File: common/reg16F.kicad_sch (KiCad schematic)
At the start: 8 parts, among them U10 SN74AHCT16374DGGR, U11 74AHC1G08

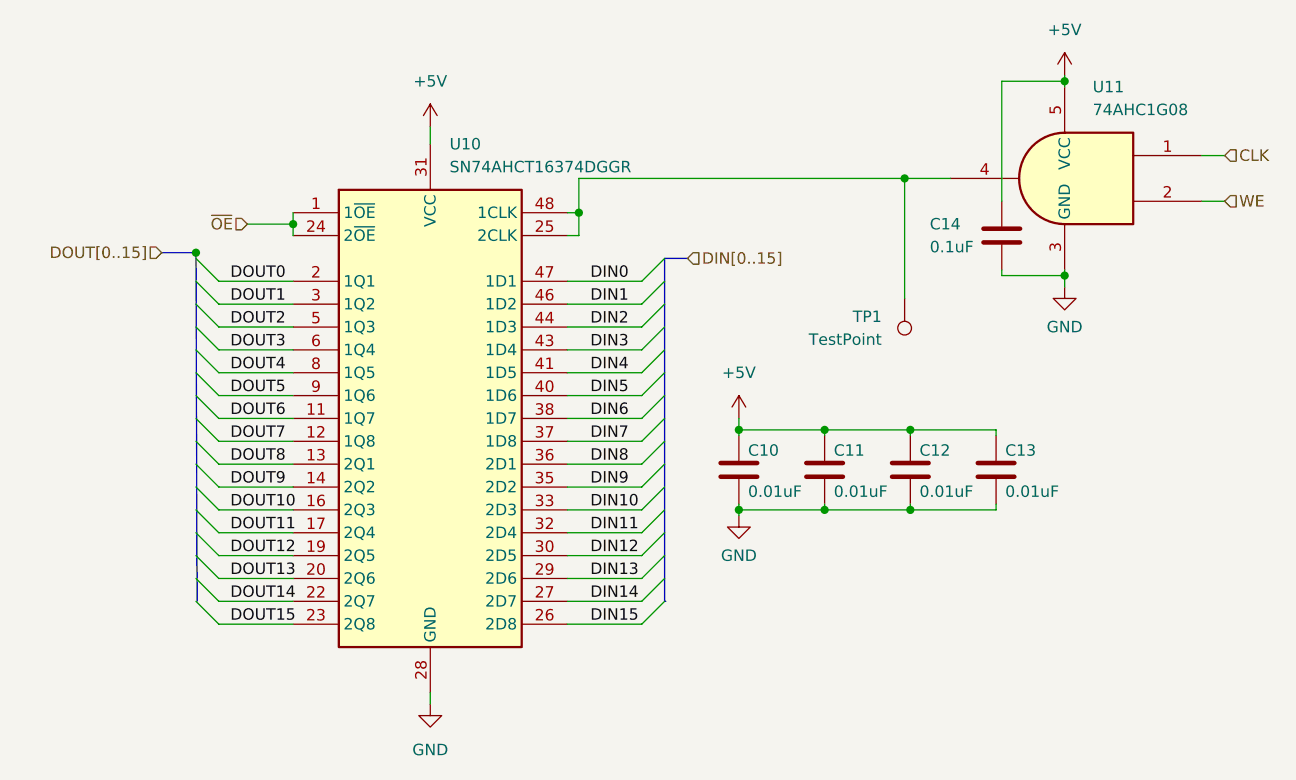
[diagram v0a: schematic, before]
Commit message: Cleanup, added photos and README overhaul
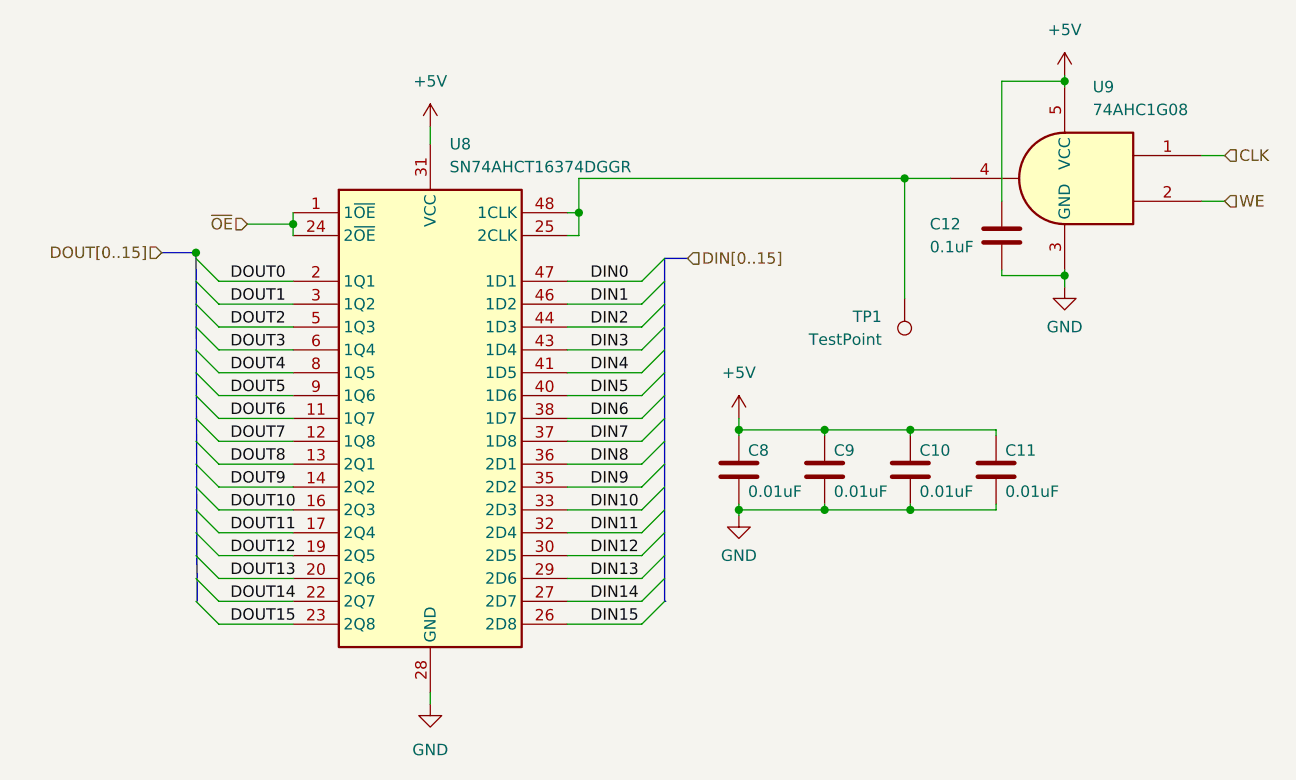
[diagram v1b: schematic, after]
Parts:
- renumbered C12 to C10, C13 to C11, C14 to C12, C10 to C8, C11 to C9, U10 to U8, U11 to U9
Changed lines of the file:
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@@
 		(dnp no)
 		(fields_autoplaced yes)
-		(property "Reference" "#PWR0103"
+		(property "Reference" "#PWR0105"
 			(at 141.605 95.885 0)
 			(effects
@@
 		)
 		(instances
+			(project "Control"
+				(path "/0a4a6030-43dc-471b-9d34-a62eb343ab9f/e990d385-57d0-437e-97d9-9478b04714cc"
+					(reference "#PWR0105")
+					(unit 1)
+				)
+			)
 			(project "Memory Controller"
 				(path "/a2e955d2-87ce-495b-9d0c-0c0d88eefe1c/7032f906-79dd-4ab6-9425-af002e61fd88"
@@
 		(dnp no)
 		(fields_autoplaced yes)
-		(property "Reference" "#PWR023"
+		(property "Reference" "#PWR020"
 			(at 107.315 116.84 0)
 			(effects
@@
 		(on_board yes)
 		(dnp no)
-		(property "Reference" "C12"
+		(property "Reference" "C10"
 			(at 161.671 82.296 0)
 			(effects
@@
 		)
 		(instances
+			(project "Control"
+				(path "/0a4a6030-43dc-471b-9d34-a62eb343ab9f/e990d385-57d0-437e-97d9-9478b04714cc"
+					(reference "C10")
+					(unit 1)
+				)
+			)
 			(project "Memory Controller"
 				(path "/a2e955d2-87ce-495b-9d0c-0c0d88eefe1c/7032f906-79dd-4ab6-9425-af002e61fd88"
@@
 		(on_board yes)
 		(dnp no)
-		(property "Reference" "C10"
+		(property "Reference" "C8"
 			(at 142.621 82.296 0)
 			(effects
@@
 		)
 		(instances
+			(project "Control"
+				(path "/0a4a6030-43dc-471b-9d34-a62eb343ab9f/e990d385-57d0-437e-97d9-9478b04714cc"
+					(reference "C8")
+					(unit 1)
+				)
+			)
 			(project "Memory Controller"
 				(path "/a2e955d2-87ce-495b-9d0c-0c0d88eefe1c/7032f906-79dd-4ab6-9425-af002e61fd88"
@@
 		(dnp no)
 		(fields_autoplaced yes)
-		(property "Reference" "U10"
+		(property "Reference" "U8"
 			(at 109.4583 48.26 0)
 			(effects
@@
 		(on_board yes)
 		(dnp no)
-		(property "Reference" "C14"
+		(property "Reference" "C12"
 			(at 162.814 57.15 0)
 			(effects
@@
 		)
 		(instances
+			(project "Control"
+				(path "/0a4a6030-43dc-471b-9d34-a62eb343ab9f/e990d385-57d0-437e-97d9-9478b04714cc"
+					(reference "C12")
+					(unit 1)
+				)
+			)
 			(project "Memory Controller"
 				(path "/a2e955d2-87ce-495b-9d0c-0c0d88eefe1c/7032f906-79dd-4ab6-9425-af002e61fd88"
@@
 		(on_board yes)
 		(dnp no)
-		(property "Reference" "C13"
+		(property "Reference" "C11"
 			(at 171.196 82.296 0)
 			(effects
@@
 		)
 		(instances
+			(project "Control"
+				(path "/0a4a6030-43dc-471b-9d34-a62eb343ab9f/e990d385-57d0-437e-97d9-9478b04714cc"
+					(reference "C11")
+					(unit 1)
+				)
+			)
 			(project "Memory Controller"
 				(path "/a2e955d2-87ce-495b-9d0c-0c0d88eefe1c/7032f906-79dd-4ab6-9425-af002e61fd88"
@@
 		)
 		(instances
+			(project "Control"
+				(path "/0a4a6030-43dc-471b-9d34-a62eb343ab9f/e990d385-57d0-437e-97d9-9478b04714cc"
+					(reference "TP1")
+					(unit 1)
+				)
+			)
 			(project "Memory Controller"
 				(path "/a2e955d2-87ce-495b-9d0c-0c0d88eefe1c/7032f906-79dd-4ab6-9425-af002e61fd88"
@@
 		(dnp no)
 		(fields_autoplaced yes)
-		(property "Reference" "#PWR0102"
+		(property "Reference" "#PWR0104"
 			(at 107.315 50.165 0)
 			(effects
@@
 		)
 		(instances
+			(project "Control"
+				(path "/0a4a6030-43dc-471b-9d34-a62eb343ab9f/e990d385-57d0-437e-97d9-9478b04714cc"
+					(reference "#PWR0104")
+					(unit 1)
+				)
+			)
 			(project "Memory Controller"
 				(path "/a2e955d2-87ce-495b-9d0c-0c0d88eefe1c/7032f906-79dd-4ab6-9425-af002e61fd88"
@@
 		(on_board yes)
 		(dnp no)
-		(property "Reference" "C11"
+		(property "Reference" "C9"
 			(at 152.146 82.296 0)
 			(effects
@@
 		)
 		(instances
+			(project "Control"
+				(path "/0a4a6030-43dc-471b-9d34-a62eb343ab9f/e990d385-57d0-437e-97d9-9478b04714cc"
+					(reference "C9")
+					(unit 1)
+				)
+			)
 			(project "Memory Controller"
 				(path "/a2e955d2-87ce-495b-9d0c-0c0d88eefe1c/7032f906-79dd-4ab6-9425-af002e61fd88"
@@
 		(dnp no)
 		(fields_autoplaced yes)
-		(property "Reference" "#PWR0104"
+		(property "Reference" "#PWR0106"
 			(at 177.8 44.45 0)
 			(effects
@@
 		)
 		(instances
+			(project "Control"
+				(path "/0a4a6030-43dc-471b-9d34-a62eb343ab9f/e990d385-57d0-437e-97d9-9478b04714cc"
+					(reference "#PWR0106")
+					(unit 1)
+				)
+			)
 			(project "Memory Controller"
 				(path "/a2e955d2-87ce-495b-9d0c-0c0d88eefe1c/7032f906-79dd-4ab6-9425-af002e61fd88"
@@
 		(dnp no)
 		(fields_autoplaced yes)
-		(property "Reference" "#PWR0105"
+		(property "Reference" "#PWR0107"
 			(at 177.8 70.485 0)
 			(effects
@@
 		)
 		(instances
+			(project "Control"
+				(path "/0a4a6030-43dc-471b-9d34-a62eb343ab9f/e990d385-57d0-437e-97d9-9478b04714cc"
+					(reference "#PWR0107")
+					(unit 1)
+				)
+			)
 			(project "Memory Controller"
 				(path "/a2e955d2-87ce-495b-9d0c-0c0d88eefe1c/7032f906-79dd-4ab6-9425-af002e61fd88"
@@
 		(dnp no)
 		(fields_autoplaced yes)
-		(property "Reference" "U11"
+		(property "Reference" "U9"
 			(at 180.9181 41.91 0)
 			(effects
@@
 		)
 		(instances
+			(project "Control"
+				(path "/0a4a6030-43dc-471b-9d34-a62eb343ab9f/e990d385-57d0-437e-97d9-9478b04714cc"
+					(reference "U9")
+					(unit 1)
+				)
+			)
 			(project "Memory Controller"
 				(path "/a2e955d2-87ce-495b-9d0c-0c0d88eefe1c/7032f906-79dd-4ab6-9425-af002e61fd88"
@@
 		(dnp no)
 		(fields_autoplaced yes)
-		(property "Reference" "#PWR0101"
+		(property "Reference" "#PWR0103"
 			(at 141.605 82.55 0)
 			(effects
@@
 		)
 		(instances
+			(project "Control"
+				(path "/0a4a6030-43dc-471b-9d34-a62eb343ab9f/e990d385-57d0-437e-97d9-9478b04714cc"
+					(reference "#PWR0103")
+					(unit 1)
+				)
+			)
 			(project "Memory Controller"
 				(path "/a2e955d2-87ce-495b-9d0c-0c0d88eefe1c/7032f906-79dd-4ab6-9425-af002e61fd88"
